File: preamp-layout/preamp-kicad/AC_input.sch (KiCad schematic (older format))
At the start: 4 parts, among them SW1 SW_SPST

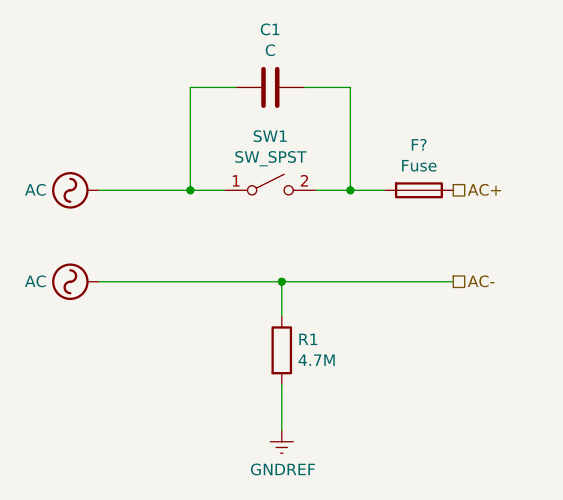
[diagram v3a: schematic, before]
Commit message: IO layout cleanup
Changed location of bal/unbal buffers from selector board to daughter board. Generalized IO PCB to accept daughter boards, not specific to connector type or bal/unbal. The idea is that as many unbalanced RCAs can be populated on the main IO board as desired and jumper cables can also be added to daughter boards as needed for different kinds of IO, but the interface to the selector board does not need to change to allow this.
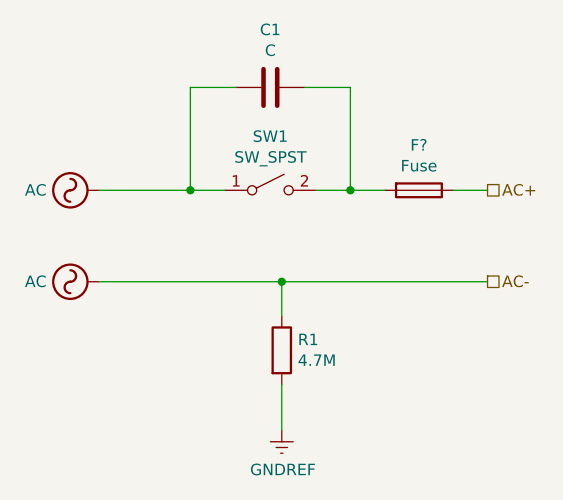
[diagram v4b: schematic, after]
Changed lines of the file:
@@
 EESchema Schematic File Version 4
-LIBS:preamp-cache
 EELAYER 30 0
 EELAYER END
 $Descr A4 11693 8268
 encoding utf-8
-Sheet 2 13
+Sheet 2 14
 Title ""
 Date ""
@@
 	5750 3400 5600 3400
 Connection ~ 5600 3400
+Connection ~ 5300 3800
+Text HLabel 6200 3400 2    50   UnSpc ~ 0
+AC+
+Text HLabel 6200 3800 2    50   UnSpc ~ 0
+AC-
 Wire Wire Line
-	5300 3800 6050 3800
-Connection ~ 5300 3800
-Text HLabel 6050 3400 2    50   UnSpc ~ 0
-AC+
-Text HLabel 6050 3800 2    50   UnSpc ~ 0
-AC-
+	6050 3400 6200 3400
+Wire Wire Line
+	5300 3800 6200 3800
 $EndSCHEMATC
